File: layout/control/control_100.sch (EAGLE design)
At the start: 61 parts, among them IC1 STM32F103C8T, IC2 LP2985-SOT23-5, IC3 IC_USBLC6-2, IC4 IC_USBLC6-2, IC5 LT1619ES8, IC6 LP2985-SOT23-5, IC7 IRF7470, T1 LPISR, X1 MINI-USB-SCHIELD-32005-201, Y1 532-CRYSTAL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

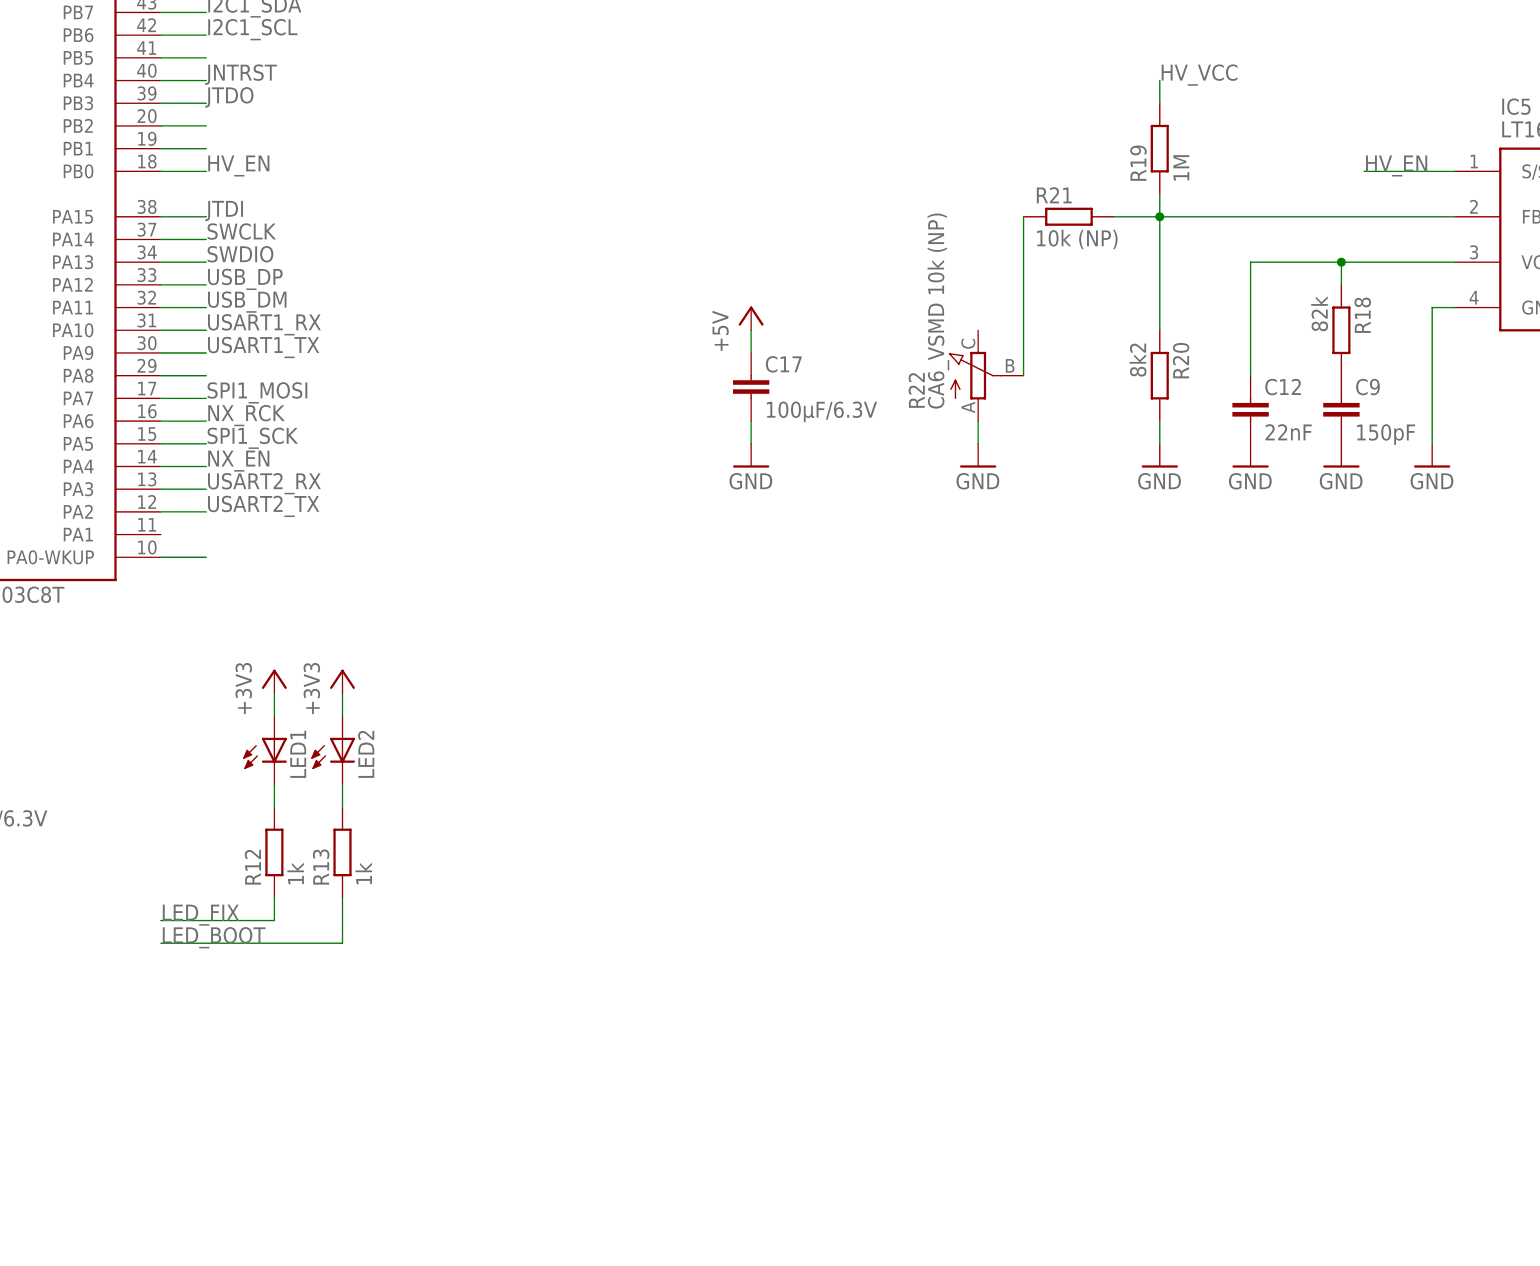
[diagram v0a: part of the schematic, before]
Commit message: Changed structure, added HM-11
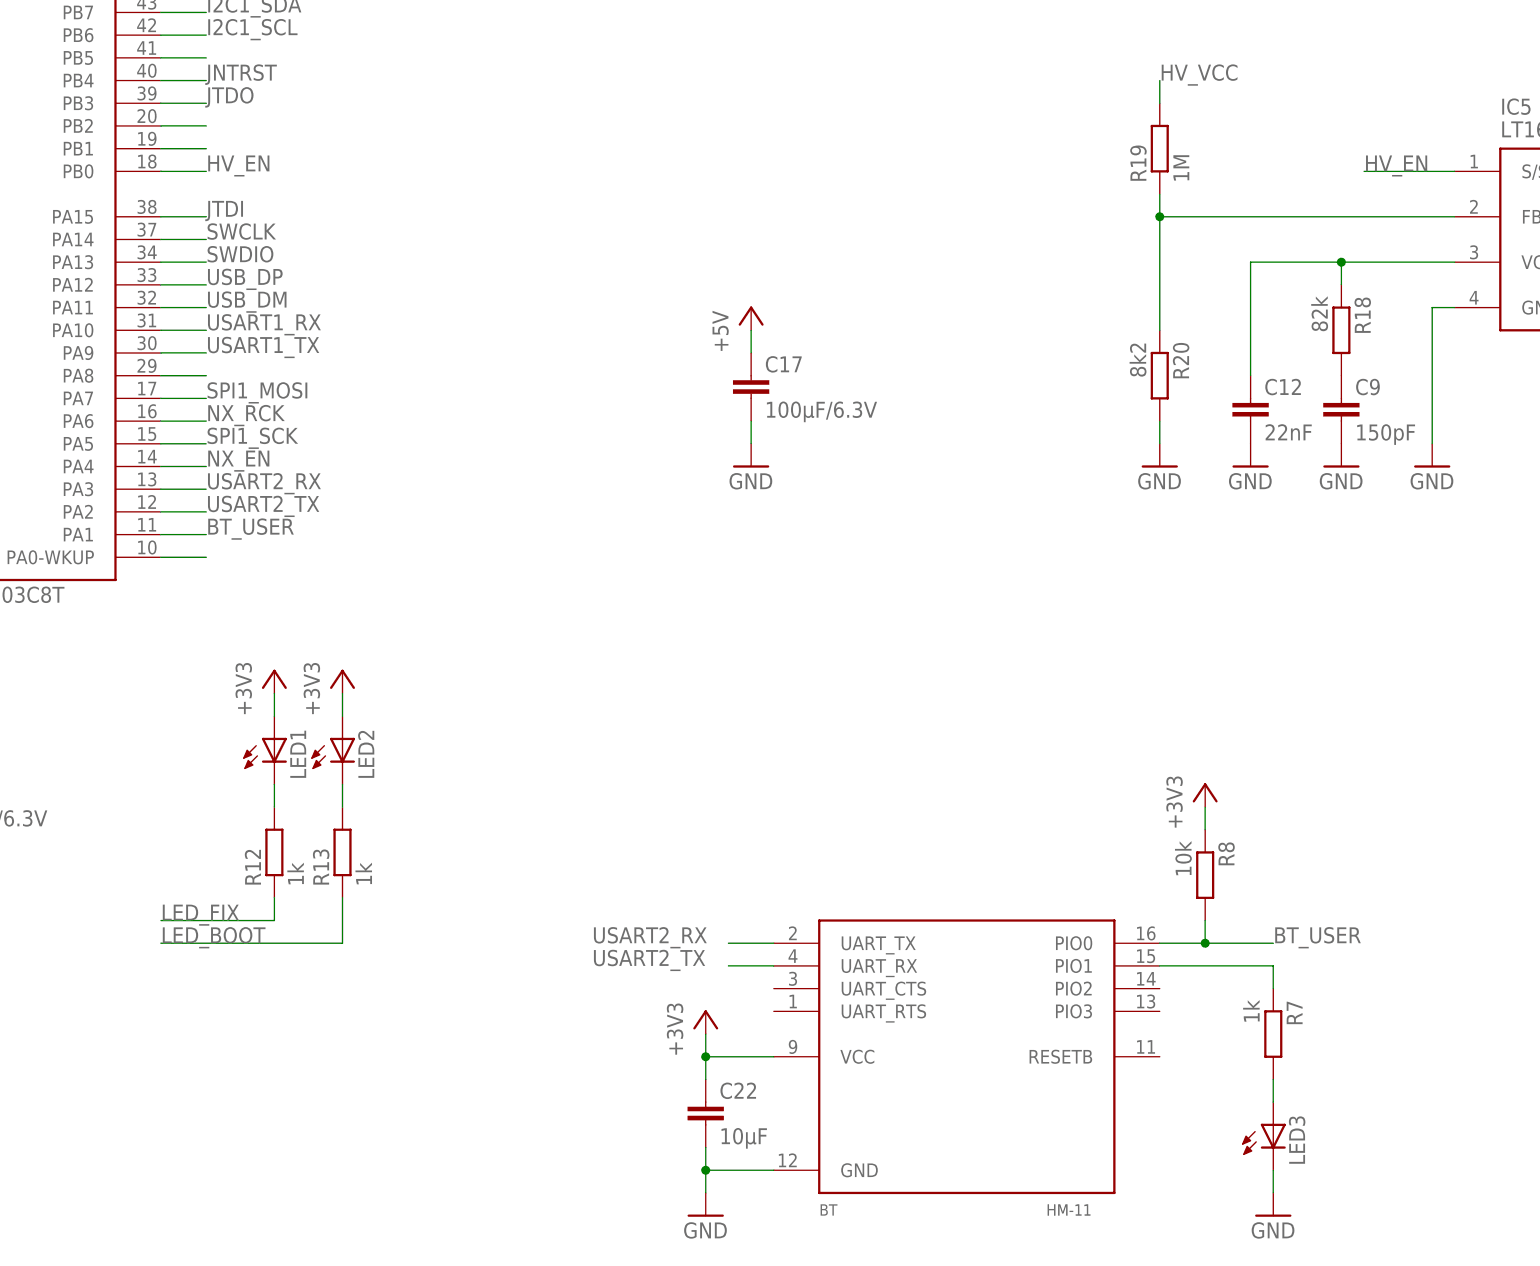
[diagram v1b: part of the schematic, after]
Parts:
- removed R21: 10k (NP), rcl:R-EU_R0603
- removed R22: CA6_VSMD 10k (NP), acp:CA6_VSMD
- added BT: HM-11, bt:HM-11
- added C22: 10µF, rcl:C-EUC0603
- added LED3: (no value), led:LEDCHIP-LED0603
- added R7: 1k, rcl:R-EU_R0603
- added R8: 10k, rcl:R-EU_R0603
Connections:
- removed net N$21: R21.1, R22.S
- new net BT_USER: BT.PIO0, IC1MCU.PA1, R8.2
- new net N$26: BT.PIO1, R7.1
- new net N$27: LED3.A, R7.2
- net +3V3: now also BT.VCC, C22.1, R8.1
- net GND: now also BT.GND, C22.2, LED3.C; no longer R22.A
- net N$17: no longer R21.2
- net USART2_RX: now also BT.UART_TX
- net USART2_TX: now also BT.UART_RX
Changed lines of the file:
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@@
 <part name="TP3" library="microbuilder" deviceset="TESTPOINT" device="ROUND2MM"/>
 <part name="TP4" library="microbuilder" deviceset="TESTPOINT" device="ROUND2MM"/>
-<part name="R22" library="acp" deviceset="CA6" device="_VSMD" value="CA6_VSMD 10k (NP)"/>
-<part name="GND32" library="supply1" deviceset="GND" device=""/>
-<part name="R21" library="rcl" deviceset="R-EU_" device="R0603" value="10k (NP)"/>
 <part name="ISP" library="tactile-switch" deviceset="TACT-SWITCH-40-40" device=""/>
 <part name="IC1" library="micro-stm_v3" deviceset="STM32F103C*T" device="" technology="8"/>
@@
 <part name="R6" library="rcl" deviceset="R-EU_" device="R0603" value="1k5"/>
 <part name="+3V1" library="supply1" deviceset="+3V3" device=""/>
+<part name="BT" library="bt" deviceset="HM-11" device=""/>
+<part name="GND32" library="supply1" deviceset="GND" device=""/>
+<part name="C22" library="rcl" deviceset="C-EU" device="C0603" value="10µF"/>
+<part name="+3V4" library="supply1" deviceset="+3V3" device=""/>
+<part name="LED3" library="led" deviceset="LED" device="CHIP-LED0603"/>
+<part name="R7" library="rcl" deviceset="R-EU_" device="R0603" value="1k"/>
+<part name="R8" library="rcl" deviceset="R-EU_" device="R0603" value="10k"/>
+<part name="GND33" library="supply1" deviceset="GND" device=""/>
+<part name="+3V6" library="supply1" deviceset="+3V3" device=""/>
 </parts>
 <sheets>
@@
 <instance part="TP3" gate="G$1" x="449.58" y="139.7" rot="R270"/>
 <instance part="TP4" gate="G$1" x="449.58" y="134.62" rot="R270"/>
-<instance part="R22" gate="G$1" x="327.66" y="104.14"/>
-<instance part="GND32" gate="1" x="327.66" y="93.98"/>
-<instance part="R21" gate="G$1" x="337.82" y="121.92"/>
 <instance part="ISP" gate="G$1" x="167.64" y="55.88" rot="R90"/>
 <instance part="IC1" gate="MCU" x="213.36" y="124.46"/>
@@
 <instance part="R6" gate="G$1" x="48.26" y="142.24" rot="MR90"/>
 <instance part="+3V1" gate="G$1" x="48.26" y="132.08" rot="MR180"/>
+<instance part="BT" gate="G$1" x="309.88" y="12.7"/>
+<instance part="GND32" gate="1" x="297.18" y="10.16"/>
+<instance part="C22" gate="G$1" x="297.18" y="22.86"/>
+<instance part="+3V4" gate="G$1" x="297.18" y="33.02"/>
+<instance part="LED3" gate="G$1" x="360.68" y="20.32"/>
+<instance part="R7" gate="G$1" x="360.68" y="30.48" rot="R270"/>
+<instance part="R8" gate="G$1" x="353.06" y="48.26" rot="R270"/>
+<instance part="GND33" gate="1" x="360.68" y="10.16"/>
+<instance part="+3V6" gate="G$1" x="353.06" y="58.42"/>
 </instances>
 <busses>
@@
 </segment>
 <segment>
-<pinref part="R22" gate="G$1" pin="A"/>
-<pinref part="GND32" gate="1" pin="GND"/>
-<wire x1="327.66" y1="99.06" x2="327.66" y2="96.52" width="0.1524" layer="91"/>
-</segment>
-<segment>
 <pinref part="C1" gate="G$1" pin="2"/>
 <pinref part="GND13" gate="1" pin="GND"/>
@@
 <wire x1="185.42" y1="83.82" x2="185.42" y2="81.28" width="0.1524" layer="91"/>
 </segment>
+<segment>
+<pinref part="BT" gate="G$1" pin="GND"/>
+<pinref part="C22" gate="G$1" pin="2"/>
+<wire x1="304.8" y1="15.24" x2="297.18" y2="15.24" width="0.1524" layer="91"/>
+<wire x1="297.18" y1="15.24" x2="297.18" y2="17.78" width="0.1524" layer="91"/>
+<pinref part="GND32" gate="1" pin="GND"/>
+<wire x1="297.18" y1="15.24" x2="297.18" y2="12.7" width="0.1524" layer="91"/>
+<junction x="297.18" y="15.24"/>
+</segment>
+<segment>
+<pinref part="LED3" gate="G$1" pin="C"/>
+<pinref part="GND33" gate="1" pin="GND"/>
+<wire x1="360.68" y1="12.7" x2="360.68" y2="15.24" width="0.1524" layer="91"/>
+</segment>
 </net>
 <net name="+5V" class="0">
@@
 <pinref part="+3V1" gate="G$1" pin="+3V3"/>
 </segment>
+<segment>
+<pinref part="BT" gate="G$1" pin="VCC"/>
+<pinref part="C22" gate="G$1" pin="1"/>
+<wire x1="304.8" y1="27.94" x2="297.18" y2="27.94" width="0.1524" layer="91"/>
+<wire x1="297.18" y1="27.94" x2="297.18" y2="25.4" width="0.1524" layer="91"/>
+<pinref part="+3V4" gate="G$1" pin="+3V3"/>
+<wire x1="297.18" y1="30.48" x2="297.18" y2="27.94" width="0.1524" layer="91"/>
+<junction x="297.18" y="27.94"/>
+</segment>
+<segment>
+<pinref part="R8" gate="G$1" pin="1"/>
+<pinref part="+3V6" gate="G$1" pin="+3V3"/>
+<wire x1="353.06" y1="55.88" x2="353.06" y2="53.34" width="0.1524" layer="91"/>
+</segment>
 </net>
 <net name="LED_FIX" class="0">
@@
 <wire x1="347.98" y1="109.22" x2="347.98" y2="121.92" width="0.1524" layer="91"/>
 <pinref part="R19" gate="G$1" pin="1"/>
-<pinref part="R21" gate="G$1" pin="2"/>
-<wire x1="342.9" y1="121.92" x2="347.98" y2="121.92" width="0.1524" layer="91"/>
 </segment>
 </net>
@@
 <pinref part="D3" gate="G$1" pin="A"/>
 <wire x1="469.9" y1="144.78" x2="474.98" y2="144.78" width="0.1524" layer="91"/>
-</segment>
-</net>
-<net name="N$21" class="0">
-<segment>
-<pinref part="R21" gate="G$1" pin="1"/>
-<pinref part="R22" gate="G$1" pin="S"/>
-<wire x1="332.74" y1="121.92" x2="332.74" y2="104.14" width="0.1524" layer="91"/>
 </segment>
 </net>
@@
 <label x="241.3" y="88.9" size="1.778" layer="95"/>
 </segment>
+<segment>
+<pinref part="BT" gate="G$1" pin="UART_RX"/>
+<wire x1="304.8" y1="38.1" x2="299.72" y2="38.1" width="0.1524" layer="91"/>
+<label x="284.48" y="38.1" size="1.778" layer="95"/>
+</segment>
 </net>
 <net name="USART2_RX" class="0">
@@
 <wire x1="236.22" y1="91.44" x2="241.3" y2="91.44" width="0.1524" layer="91"/>
 <label x="241.3" y="91.44" size="1.778" layer="95"/>
+</segment>
+<segment>
+<pinref part="BT" gate="G$1" pin="UART_TX"/>
+<wire x1="304.8" y1="40.64" x2="299.72" y2="40.64" width="0.1524" layer="91"/>
+<label x="284.48" y="40.64" size="1.778" layer="95"/>
 </segment>
 </net>
@@
 </segment>
 </net>
+<net name="N$26" class="0">
+<segment>
+<pinref part="BT" gate="G$1" pin="PIO1"/>
+<pinref part="R7" gate="G$1" pin="1"/>
+<wire x1="347.98" y1="38.1" x2="360.68" y2="38.1" width="0.1524" layer="91"/>
+<wire x1="360.68" y1="38.1" x2="360.68" y2="35.56" width="0.1524" layer="91"/>
+</segment>
+</net>
+<net name="N$27" class="0">
+<segment>
+<pinref part="R7" gate="G$1" pin="2"/>
+<pinref part="LED3" gate="G$1" pin="A"/>
+<wire x1="360.68" y1="22.86" x2="360.68" y2="25.4" width="0.1524" layer="91"/>
+</segment>
+</net>
+<net name="BT_USER" class="0">
+<segment>
+<pinref part="BT" gate="G$1" pin="PIO0"/>
+<pinref part="R8" gate="G$1" pin="2"/>
+<wire x1="347.98" y1="40.64" x2="353.06" y2="40.64" width="0.1524" layer="91"/>
+<wire x1="353.06" y1="40.64" x2="353.06" y2="43.18" width="0.1524" layer="91"/>
+<wire x1="353.06" y1="40.64" x2="360.68" y2="40.64" width="0.1524" layer="91"/>
+<junction x="353.06" y="40.64"/>
+<label x="360.68" y="40.64" size="1.778" layer="95"/>
+</segment>
+<segment>
+<pinref part="IC1" gate="MCU" pin="PA1"/>
+<wire x1="236.22" y1="86.36" x2="241.3" y2="86.36" width="0.1524" layer="91"/>
+<label x="241.3" y="86.36" size="1.778" layer="95"/>
+</segment>
+</net>
